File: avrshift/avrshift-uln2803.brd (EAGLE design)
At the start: 45.7 x 49.5 mm, 21 parts, among them IC1 AT90S2313S, IC2 7805TV, IC3 ULN2803A, IC4 ULN2803A

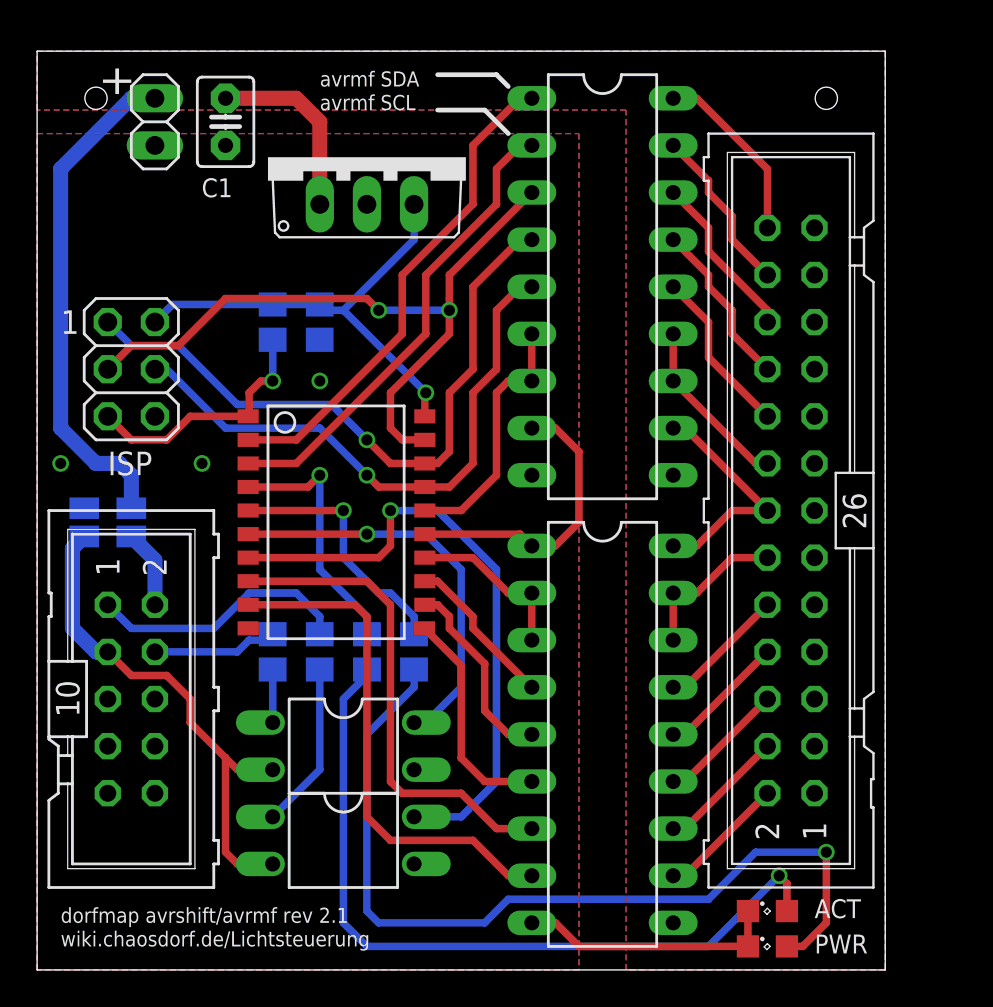
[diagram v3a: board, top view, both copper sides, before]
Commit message: add more names, VIAs and OSHW logo
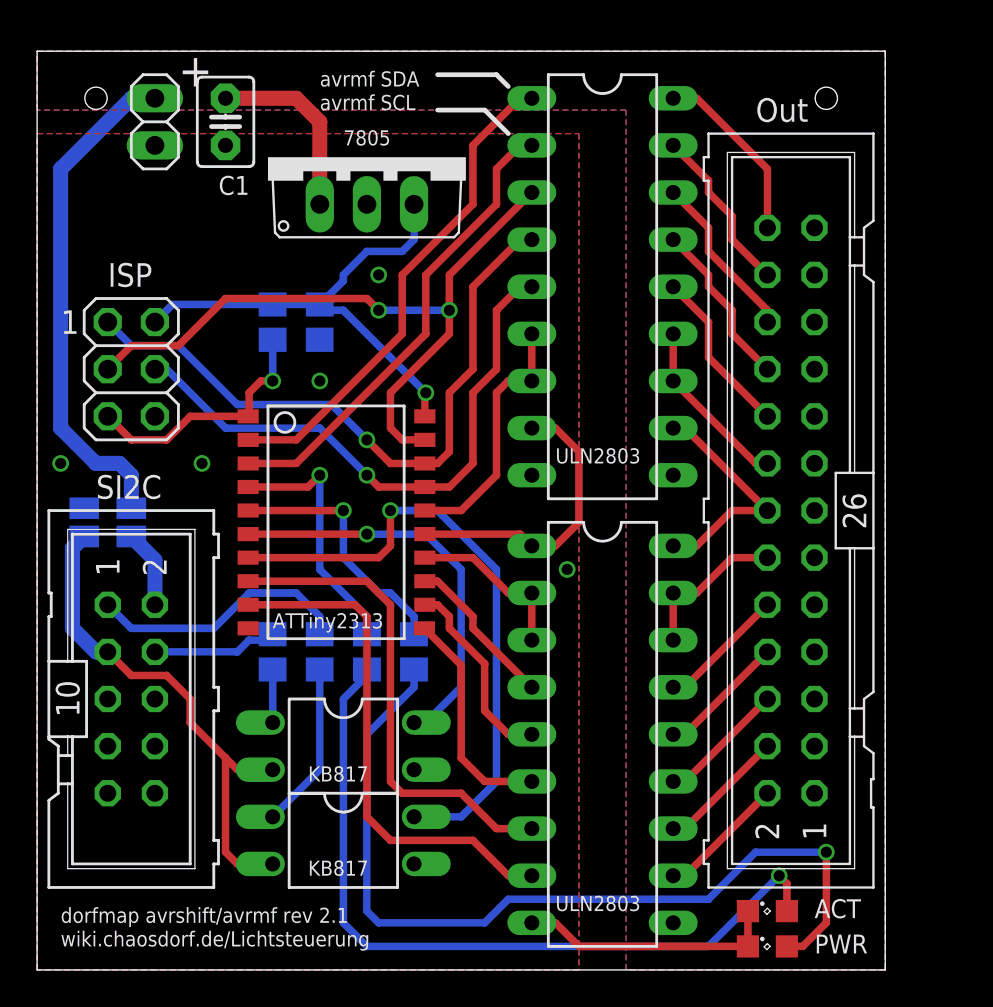
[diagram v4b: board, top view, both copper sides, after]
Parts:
- added GOLD_ORB_SM1: OSHWLOGO_GOLD_ORB_SM, bfl:OSHW2
- SV3: value (none) -> output
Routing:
- net 5V: track 25.6 -> 26.9 mm
- net GND: vias 3 -> 5
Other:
- board text added: "7805"
- board text added: "ATTiny2313"
- board text added: "KB817"
- board text added: "Out"
- board text added: "SI2C"
- board text added: "ULN2803"
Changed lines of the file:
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@@
 <layer number="48" name="Document" color="7" fill="1" visible="yes" active="yes"/>
 <layer number="49" name="Reference" color="7" fill="1" visible="yes" active="yes"/>
+<layer number="50" name="dxf" color="7" fill="1" visible="yes" active="yes"/>
 <layer number="51" name="tDocu" color="7" fill="1" visible="yes" active="yes"/>
 <layer number="52" name="bDocu" color="7" fill="1" visible="yes" active="yes"/>
+<layer number="53" name="tGND_GNDA" color="7" fill="9" visible="no" active="no"/>
+<layer number="54" name="bGND_GNDA" color="1" fill="9" visible="no" active="no"/>
+<layer number="56" name="wert" color="7" fill="1" visible="yes" active="yes"/>
 <layer number="91" name="Nets" color="2" fill="1" visible="no" active="no"/>
 <layer number="92" name="Busses" color="1" fill="1" visible="no" active="no"/>
@@
 <layer number="97" name="Info" color="7" fill="1" visible="no" active="no"/>
 <layer number="98" name="Guide" color="6" fill="1" visible="no" active="no"/>
+<layer number="100" name="Muster" color="7" fill="1" visible="no" active="no"/>
+<layer number="101" name="Patch_Top" color="12" fill="4" visible="yes" active="yes"/>
+<layer number="102" name="Vscore" color="7" fill="1" visible="yes" active="yes"/>
+<layer number="103" name="tMap" color="7" fill="1" visible="yes" active="yes"/>
+<layer number="104" name="Name" color="7" fill="1" visible="yes" active="yes"/>
+<layer number="105" name="tPlate" color="7" fill="1" visible="yes" active="yes"/>
+<layer number="106" name="bPlate" color="7" fill="1" visible="yes" active="yes"/>
+<layer number="107" name="Crop" color="7" fill="1" visible="yes" active="yes"/>
+<layer number="116" name="Patch_BOT" color="9" fill="4" visible="yes" active="yes"/>
+<layer number="121" name="_tsilk" color="7" fill="1" visible="yes" active="yes"/>
+<layer number="122" name="_bsilk" color="7" fill="1" visible="yes" active="yes"/>
+<layer number="125" name="_tNames" color="7" fill="1" visible="yes" active="yes"/>
+<layer number="144" name="Drill_legend" color="7" fill="1" visible="yes" active="yes"/>
+<layer number="151" name="HeatSink" color="7" fill="1" visible="yes" active="yes"/>
+<layer number="200" name="200bmp" color="1" fill="10" visible="yes" active="yes"/>
+<layer number="201" name="201bmp" color="2" fill="10" visible="yes" active="yes"/>
+<layer number="202" name="202bmp" color="3" fill="10" visible="yes" active="yes"/>
+<layer number="203" name="203bmp" color="4" fill="10" visible="yes" active="yes"/>
+<layer number="204" name="204bmp" color="5" fill="10" visible="yes" active="yes"/>
+<layer number="205" name="205bmp" color="6" fill="10" visible="yes" active="yes"/>
+<layer number="206" name="206bmp" color="7" fill="10" visible="yes" active="yes"/>
+<layer number="207" name="207bmp" color="8" fill="10" visible="yes" active="yes"/>
+<layer number="208" name="208bmp" color="9" fill="10" visible="yes" active="yes"/>
+<layer number="209" name="209bmp" color="7" fill="1" visible="yes" active="yes"/>
+<layer number="210" name="210bmp" color="7" fill="1" visible="yes" active="yes"/>
+<layer number="211" name="211bmp" color="7" fill="1" visible="yes" active="yes"/>
+<layer number="212" name="212bmp" color="7" fill="1" visible="yes" active="yes"/>
+<layer number="213" name="213bmp" color="7" fill="1" visible="yes" active="yes"/>
+<layer number="214" name="214bmp" color="7" fill="1" visible="yes" active="yes"/>
+<layer number="215" name="215bmp" color="7" fill="1" visible="yes" active="yes"/>
+<layer number="216" name="216bmp" color="7" fill="1" visible="yes" active="yes"/>
+<layer number="250" name="Descript" color="3" fill="1" visible="no" active="no"/>
+<layer number="251" name="SMDround" color="12" fill="11" visible="no" active="no"/>
+<layer number="254" name="cooling" color="7" fill="1" visible="yes" active="yes"/>
 </layers>
 <board>
@@
 <wire x1="45.72" y1="49.53" x2="0" y2="49.53" width="0" layer="20"/>
 <wire x1="0" y1="49.53" x2="0" y2="0" width="0" layer="20"/>
-<text x="5.08" y="46.99" size="1.778" layer="25" font="vector" rot="R90">+</text>
+<text x="7.62" y="47.625" size="1.778" layer="25" font="vector">+</text>
 <text x="15.24" y="21.59" size="1.016" layer="26" font="vector" rot="MR0">VCC select
 open  =ext
@@
 <hole x="42.545" y="46.99" drill="1.2"/>
 <hole x="3.175" y="46.99" drill="1.2"/>
-<text x="3.81" y="26.67" size="1.27" layer="25">ISP</text>
+<text x="3.81" y="36.83" size="1.27" layer="25">ISP</text>
 <text x="1.27" y="34.29" size="1.27" layer="25">1</text>
 <wire x1="1.27" y1="20.955" x2="1.27" y2="26.035" width="0.254" layer="26"/>
@@
 <text x="1.27" y="1.27" size="0.8128" layer="25">wiki.chaosdorf.de/Lichtsteuerung</text>
 <text x="1.27" y="2.54" size="0.8128" layer="25">dorfmap avrshift/avrmf rev 2.1</text>
+<text x="3.175" y="25.4" size="1.27" layer="25">SI2C</text>
+<text x="38.735" y="45.72" size="1.27" layer="25">Out</text>
+<text x="12.7" y="18.415" size="0.8128" layer="25">ATTiny2313</text>
+<text x="27.94" y="27.305" size="0.8128" layer="25">ULN2803</text>
+<text x="27.94" y="3.175" size="0.8128" layer="25">ULN2803</text>
+<text x="14.605" y="5.08" size="0.8128" layer="25">KB817</text>
+<text x="14.605" y="10.16" size="0.8128" layer="25">KB817</text>
+<text x="16.51" y="44.45" size="0.8128" layer="25">7805</text>
 </plain>
 <attributes>
@@
 </element>
 <element name="R1" library="rcl" package="R0805" value="1K" x="12.7" y="17.145" smashed="yes" rot="MR270">
-<attribute name="NAME" x="12.0142" y="14.859" size="1.016" layer="26" font="vector" ratio="10" rot="MR180"/>
+<attribute name="NAME" x="13.3858" y="19.431" size="1.016" layer="26" font="vector" ratio="10" rot="MR0"/>
 <attribute name="VALUE" x="14.9352" y="17.1958" size="1.27" layer="28" ratio="10" rot="MR270"/>
 </element>
 <element name="R2" library="rcl" package="R0805" value="1K" x="15.24" y="17.145" smashed="yes" rot="MR270">
-<attribute name="NAME" x="14.5542" y="14.859" size="1.016" layer="26" font="vector" ratio="10" rot="MR180"/>
+<attribute name="NAME" x="15.9258" y="19.431" size="1.016" layer="26" font="vector" ratio="10" rot="MR0"/>
 <attribute name="VALUE" x="17.4752" y="17.1958" size="1.27" layer="28" ratio="10" rot="MR270"/>
 </element>
 <element name="C1" library="capacitor-wima" package="C2.5-3" value="330nF" x="10.16" y="45.72" smashed="yes" rot="R270">
-<attribute name="NAME" x="10.541" y="42.672" size="1.016" layer="25" font="vector" ratio="10" rot="R180"/>
+<attribute name="NAME" x="9.779" y="41.783" size="1.016" layer="25" font="vector" ratio="10"/>
 <attribute name="VALUE" x="7.112" y="47.371" size="1.27" layer="27" ratio="10" rot="R270"/>
 </element>
 <element name="C2" library="rcl" package="C0805" value="100nF" x="15.24" y="34.925" smashed="yes" rot="MR270">
-<attribute name="NAME" x="14.478" y="37.719" size="1.016" layer="26" font="vector" ratio="10" rot="MR90"/>
+<attribute name="NAME" x="16.256" y="37.338" size="1.016" layer="26" font="vector" ratio="10" rot="MR0"/>
 <attribute name="VALUE" x="18.288" y="36.576" size="1.27" layer="28" ratio="10" rot="MR270"/>
 </element>
@@
 </element>
 <element name="R3" library="rcl" package="R0805" value="10K" x="12.7" y="34.925" smashed="yes" rot="MR90">
-<attribute name="NAME" x="11.811" y="37.4142" size="1.016" layer="26" font="vector" ratio="10" rot="MR90"/>
+<attribute name="NAME" x="13.3858" y="37.211" size="1.016" layer="26" font="vector" ratio="10" rot="MR0"/>
 <attribute name="VALUE" x="10.4648" y="34.8742" size="1.27" layer="28" ratio="10" rot="MR90"/>
 </element>
@@
 <attribute name="VALUE" x="10.16" y="31.75" size="1.778" layer="27" ratio="10" rot="R270"/>
 </element>
-<element name="SV3" library="con-ml" package="ML26" value="" x="40.64" y="24.765" smashed="yes" rot="R90">
+<element name="SV3" library="con-ml" package="ML26" value="output" x="40.64" y="24.765" smashed="yes" rot="R90">
 <attribute name="OC_NEWARK" value="unknown" x="40.64" y="24.765" size="1.778" layer="27" rot="R90" display="off"/>
 <attribute name="MPN" value="" x="40.64" y="24.765" size="1.778" layer="27" rot="R90" display="off"/>
@@
 <attribute name="VALUE" x="35.56" y="26.035" size="1.778" layer="27" ratio="10" rot="R90"/>
 </element>
+<element name="GOLD_ORB_SM1" library="bfl" package="OSHW2" value="OSHWLOGO_GOLD_ORB_SM" x="44.45" y="40.005" rot="MR0"/>
 </elements>
 <signals>
@@
 <via x="15.24" y="31.75" extent="1-16" drill="0.6"/>
 <via x="8.89" y="27.305" extent="1-16" drill="0.6"/>
+<via x="18.415" y="37.465" extent="1-16" drill="0.6"/>
+<via x="28.575" y="21.59" extent="1-16" drill="0.6"/>
 </signal>
 <signal name="N$4">
@@
 <wire x1="15.555" y1="35.56" x2="15.24" y2="35.875" width="0.4064" layer="16"/>
 <wire x1="20.32" y1="41.275" x2="20.32" y2="39.37" width="0.4064" layer="16"/>
-<wire x1="20.32" y1="39.37" x2="16.51" y2="35.56" width="0.4064" layer="16"/>
 <wire x1="15.24" y1="35.875" x2="12.7" y2="35.875" width="0.4064" layer="16"/>
 <wire x1="12.7" y1="35.875" x2="7.3" y2="35.875" width="0.4064" layer="16"/>
 <wire x1="7.3" y1="35.875" x2="6.35" y2="34.925" width="0.4064" layer="16"/>
+<wire x1="20.32" y1="39.37" x2="19.685" y2="38.735" width="0.4064" layer="16"/>
+<wire x1="19.685" y1="38.735" x2="17.78" y2="38.735" width="0.4064" layer="16"/>
+<wire x1="17.78" y1="38.735" x2="16.51" y2="37.465" width="0.4064" layer="16"/>
+<wire x1="16.51" y1="37.465" x2="16.51" y2="37.145" width="0.4064" layer="16"/>
+<wire x1="16.51" y1="37.145" x2="15.24" y2="35.875" width="0.4064" layer="16"/>
 </signal>
 <signal name="AVRSDA">
